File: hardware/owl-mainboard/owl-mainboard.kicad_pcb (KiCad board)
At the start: 4 copper layers, 61.8 x 79.8 mm, 117 parts, among them J101 Battery +, -, J201 USB-C, J202 EXP: GND, 3V3, A, B, J301 AMOLED FPC, J302 LRA, J303 DOCK: GND, VBUS, DET, GND, SW201 Ear left, SW202 Ear right, SW203 Beak, U101 BQ24073RGTR, U102 MAX17048G+T10, U103 TPS63802DLAR, U104 TPS22917DBVR, U201 ESP32-S3-WROOM-1-N16R8, U202 USBLC6-2SC6, U301 DRV2605LDGSR, U302 TMAG5273A2QDBVR, U303 LIS2DW12TR, U304 OPT3001DNPR, U305 LSF0204PWR, U306 XC6206P182MR, Y201 32.768kHz 12.5pF

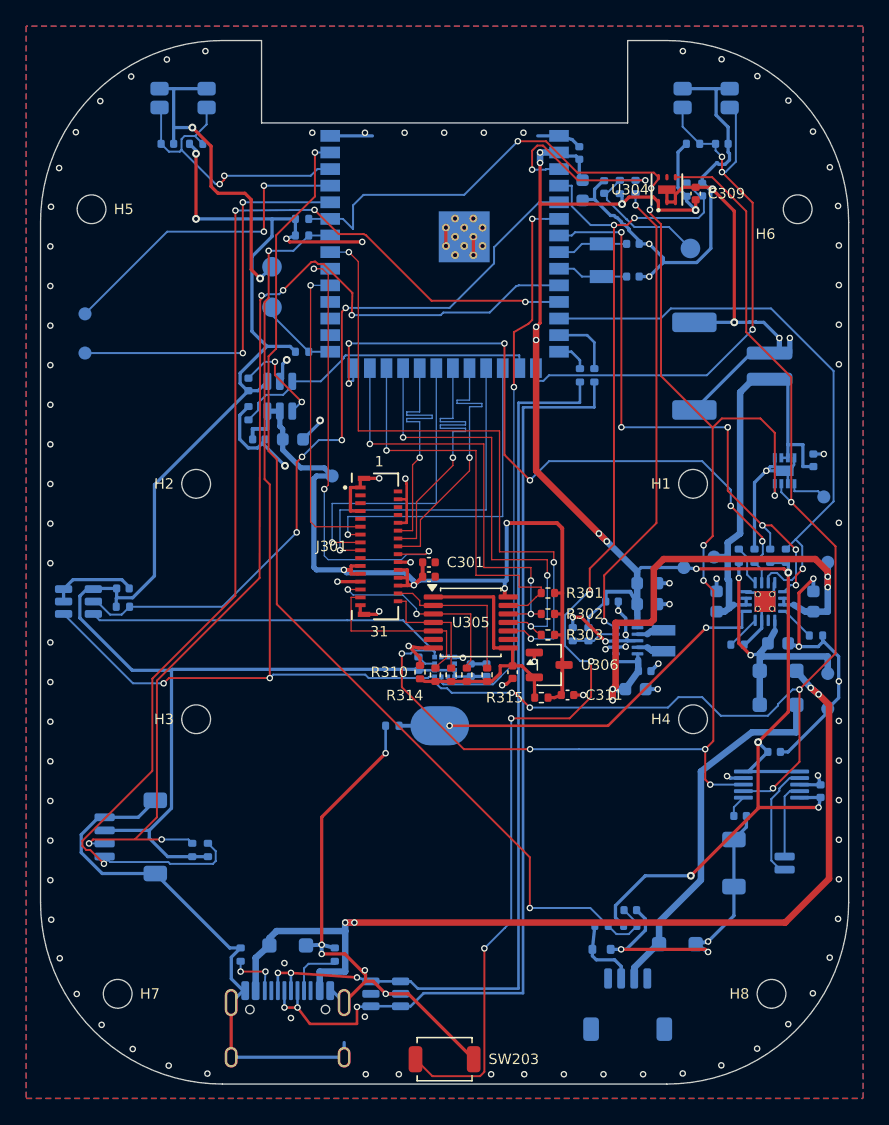
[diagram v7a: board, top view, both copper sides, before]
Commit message: feat(hardware): refill the outer pours and find the pour vias again
The moved J301 and the touch level shift change which regions of the F.Cu
and B.Cu GND pours the tracks enclose. pour_vias now holds 15 vias (9 on
F.Cu regions, 6 on B.Cu), each at the deepest spot of its region outside the
courtyards (the module's excepted, as before) and clear of other copper on
both outer layers; one of them joins C301 and C302's GND pads, which the
touch lanes fence off north of U305. The old pour via that R310's pad sat
over is gone, so R310 pad 1 has no hole clearance error.

A DRU rule keeps the pours off C312's GND pad, which reaches GND through its
own track to the via beside it (the pad has no room for a second spoke), as
C202's pad does. hw_place.py's comment states the no-pad-over-a-pour-via rule
without the old via's coordinates.

DRC (local kicad-cli 10.0.7): 0 violations, 0 unconnected, 0 parity.
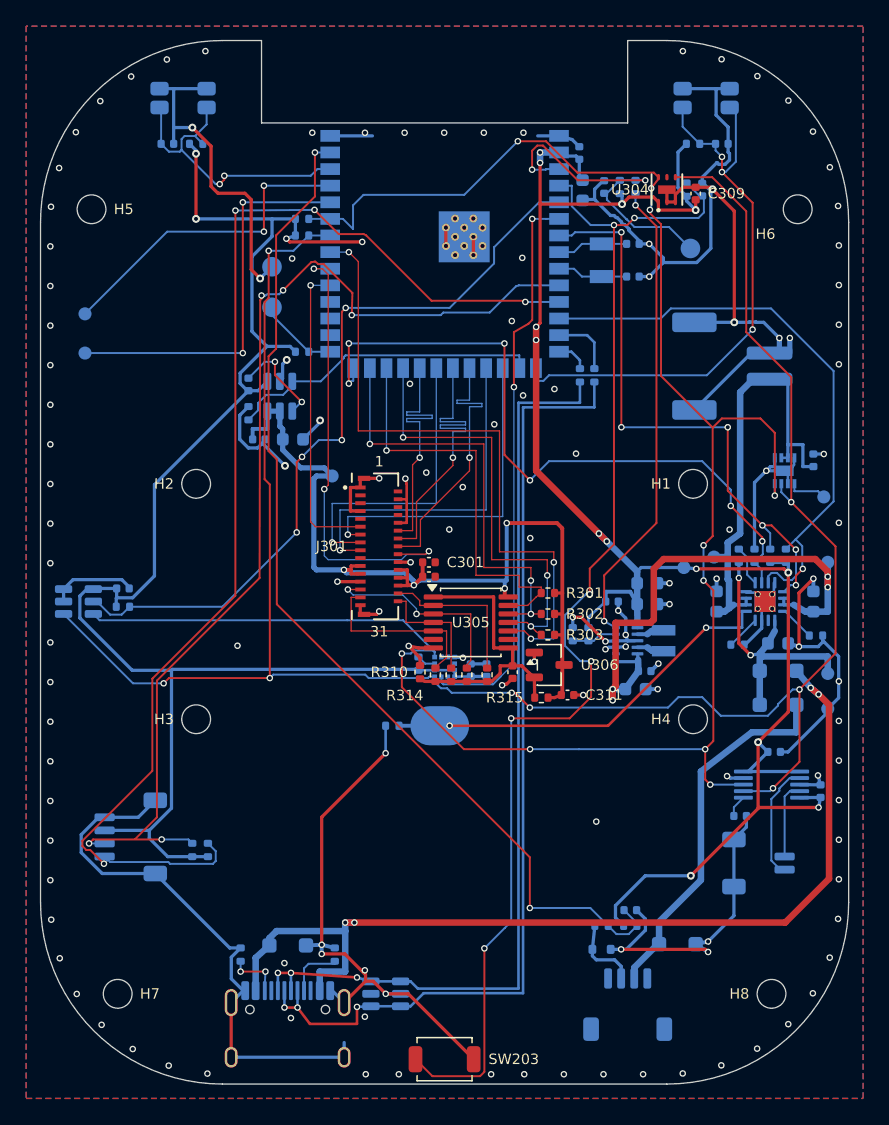
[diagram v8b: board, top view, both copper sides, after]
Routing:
- net GND: vias 117 -> 132
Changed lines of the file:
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@@
 	)
 	(via
+		(at 121.789999 94.5)
+		(size 0.5)
+		(drill 0.3)
+		(layers "F.Cu" "B.Cu")
+		(locked yes)
+		(net "GND")
+	)
+	(via
 		(at 69.85 121.31)
 		(size 0.5)
@@
 	)
 	(via
+		(at 110.05 88.69)
+		(size 0.5)
+		(drill 0.3)
+		(layers "F.Cu" "B.Cu")
+		(locked yes)
+		(net "GND")
+	)
+	(via
 		(at 69.85 115.25)
 		(size 0.5)
@@
 	)
 	(via
+		(at 106.55 95.15)
+		(size 0.5)
+		(drill 0.3)
+		(layers "F.Cu" "B.Cu")
+		(locked yes)
+		(net "GND")
+	)
+	(via
 		(at 89.88 64.15)
 		(size 0.5)
@@
 	)
 	(via
+		(at 108.4 83.75)
+		(size 0.5)
+		(drill 0.3)
+		(layers "F.Cu" "B.Cu")
+		(locked yes)
+		(net "GND")
+	)
+	(via
 		(at 91.8 98.48)
 		(size 0.5)
@@
 	)
 	(via
+		(at 103.8 86.45)
+		(size 0.5)
+		(drill 0.3)
+		(layers "F.Cu" "B.Cu")
+		(locked yes)
+		(net "GND")
+	)
+	(via
+		(at 106 84.24)
+		(size 0.5)
+		(drill 0.3)
+		(layers "F.Cu" "B.Cu")
+		(locked yes)
+		(net "GND")
+	)
+	(via
 		(at 130.15 72.77)
 		(size 0.5)
@@
 	)
 	(via
+		(at 105.14 78.55)
+		(size 0.5)
+		(drill 0.3)
+		(layers "F.Cu" "B.Cu")
+		(locked yes)
+		(net "GND")
+	)
+	(via
+		(at 88.34 73.77)
+		(size 0.5)
+		(drill 0.3)
+		(layers "F.Cu" "B.Cu")
+		(locked yes)
+		(net "GND")
+	)
+	(via
 		(at 112.3 103.05)
 		(size 0.5)
@@
 	)
 	(via
+		(at 84.16 103.38)
+		(size 0.5)
+		(drill 0.3)
+		(layers "F.Cu" "B.Cu")
+		(locked yes)
+		(net "GND")
+	)
+	(via
 		(at 109.8 101.2)
 		(size 0.5)
@@
 	)
 	(via
+		(at 101.39 91.25)
+		(size 0.5)
+		(drill 0.3)
+		(layers "F.Cu" "B.Cu")
+		(locked yes)
+		(net "GND")
+	)
+	(via
 		(at 95.49 111.6)
 		(size 0.5)
@@
 	)
 	(via
+		(at 97.35 83.35)
+		(size 0.5)
+		(drill 0.3)
+		(layers "F.Cu" "B.Cu")
+		(locked yes)
+		(net "GND")
+	)
+	(via
 		(at 117.2 98.6)
 		(size 0.5)
@@
 	)
 	(via
+		(at 98.6 90.14)
+		(size 0.5)
+		(drill 0.3)
+		(layers "F.Cu" "B.Cu")
+		(locked yes)
+		(net "GND")
+	)
+	(via
 		(at 87.7959 89.6216)
 		(size 0.6)
@@
 	)
 	(via
+		(at 100.36 94.49)
+		(size 0.5)
+		(drill 0.3)
+		(layers "F.Cu" "B.Cu")
+		(locked yes)
+		(net "GND")
+	)
+	(via
 		(at 69.85 112.22)
 		(size 0.5)
@@
 	)
 	(via
+		(at 105.94 73.72)
+		(size 0.5)
+		(drill 0.3)
+		(layers "F.Cu" "B.Cu")
+		(locked yes)
+		(net "GND")
+	)
+	(via
 		(at 118.22 57.91)
 		(size 0.5)
@@
 	)
 	(via
+		(at 111.6 116.83)
+		(size 0.5)
+		(drill 0.3)
+		(layers "F.Cu" "B.Cu")
+		(locked yes)
+		(net "GND")
+	)
+	(via
 		(at 88.25 131.85)
 		(size 0.5)
@@
 	)
 	(group "hw_route outer_pours"
-		(members "ac8f86be-881c-4d6f-a2c5-c528681cec2c" "f3e6a354-681a-4754-a09e-0c323c67f7ec")
+		(members "86404f77-546c-459c-8dc2-3387a04d416f" "e7e0ab9b-7c64-4906-ba76-85784430e1a0")
+	)
+	(group "hw_route pour_vias"
+		(members "02bd42d3-77cc-4641-a3c0-fdd8a6ae52f5" "1454e431-519d-4b23-b005-9927666b4221"
+			"6ac2a4f7-f081-48fa-bac2-8af1ecb56a30" "803c358e-7c33-4d8d-ae3c-be21a27130e9"
+			"94e6d124-a284-4e41-b288-6a727aa0cc20" "94e80337-e9bb-4652-ac2b-9cf4b1b0fc7d"
+			"a4b2fff0-23cf-49f1-81e8-6e8559952058" "a7c29449-826f-4cd9-a33d-8e091c5c892c"
+			"c7162fdc-01f5-49b2-8a3f-fb3c1e1aa46c" "ce5c548f-fb3a-4b43-939d-24473c48b67d"
+			"d259b685-6cb1-41f8-a16a-eaa3222ebd86" "dad59ab7-e7a0-4a72-b033-b52afef19588"
+			"e25aee06-c3fd-4b65-83a1-6196166f1eda" "ed196cd4-453f-40dd-8226-011db6e5e6bc"
+			"f3478be7-f731-4176-9ba2-50e9c3d437d0"
+		)
 	)
 	(group "hw_route tps_pg"
